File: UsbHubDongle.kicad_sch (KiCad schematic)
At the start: 46 parts, among them J1 USB_C_Receptacle_USB2.0, P1 USB_C_Plug, U1 AP7375-33W5-7, U2 USB2422, Y1 24MHz

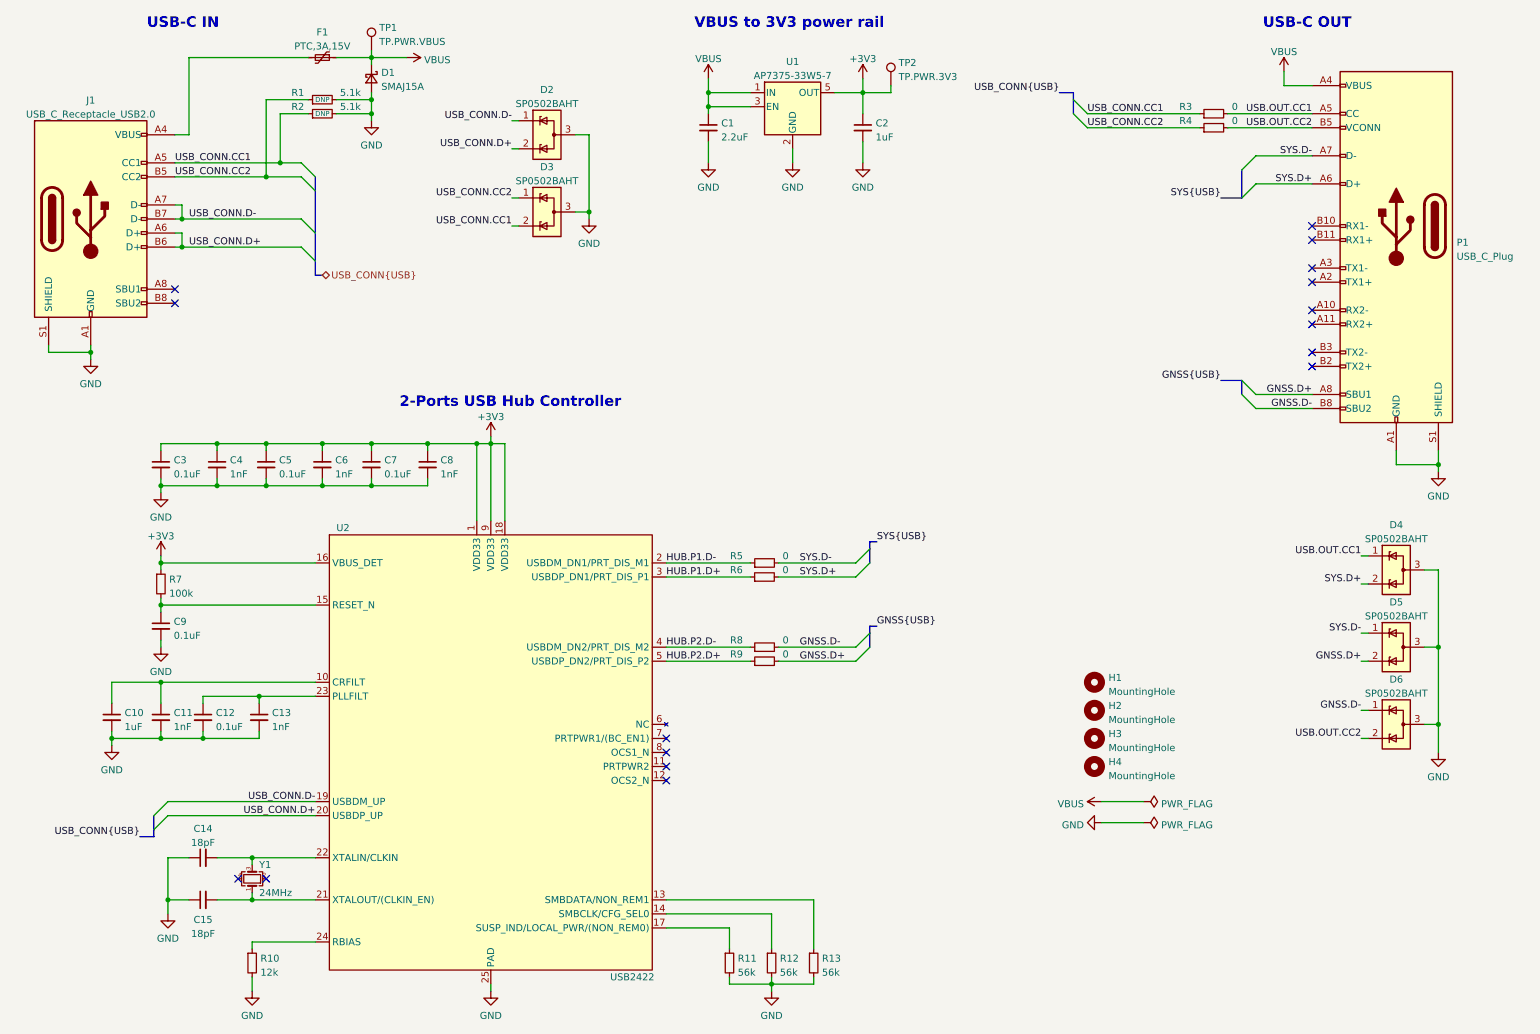
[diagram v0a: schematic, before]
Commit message: improve the differential pair lines, and increase the min via holes size from 0,2 to 0,3mm
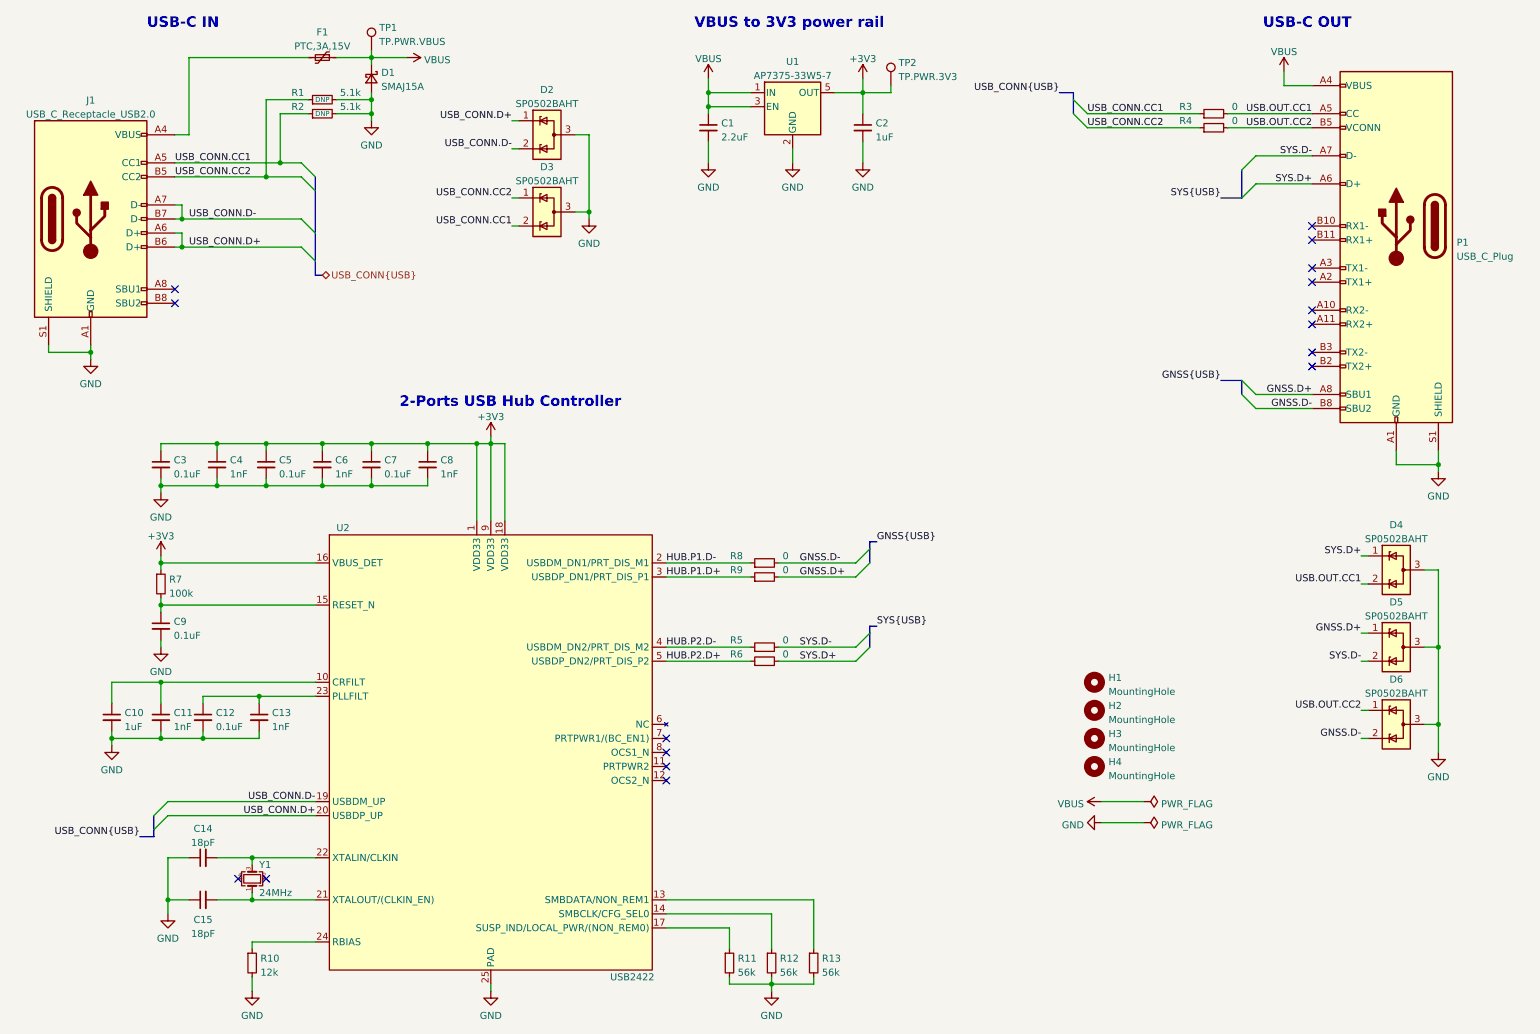
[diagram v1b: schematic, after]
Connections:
- net GNSS.D+: now also D5.1 (K); no longer D5.2 (K)
- net GNSS.D-: now also D6.2 (K); no longer D6.1 (K)
- net HUB.P1.D+: now also R9.1; no longer R6.1
- net HUB.P1.D-: now also R8.1; no longer R5.1
- net HUB.P2.D+: now also R6.1; no longer R9.1
- net HUB.P2.D-: now also R5.1; no longer R8.1
- net SYS.D+: now also D4.1 (K); no longer D4.2 (K)
- net SYS.D-: now also D5.2 (K); no longer D5.1 (K)
- net USB.OUT.CC1: now also D4.2 (K); no longer D4.1 (K)
- net USB.OUT.CC2: now also D6.1 (K); no longer D6.2 (K)
- net USB_CONN.D+: now also D2.1 (K); no longer D2.2 (K)
- net USB_CONN.D-: now also D2.2 (K); no longer D2.1 (K)
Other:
- moved on the sheet: R5, R6, R8, R9
